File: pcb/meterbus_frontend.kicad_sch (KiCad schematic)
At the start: 32 parts, among them J2 6P6C, Q1 SQ2308CES-T1_GE3, U1 L7805, U2 74HC132, U3 ISO6721RBD

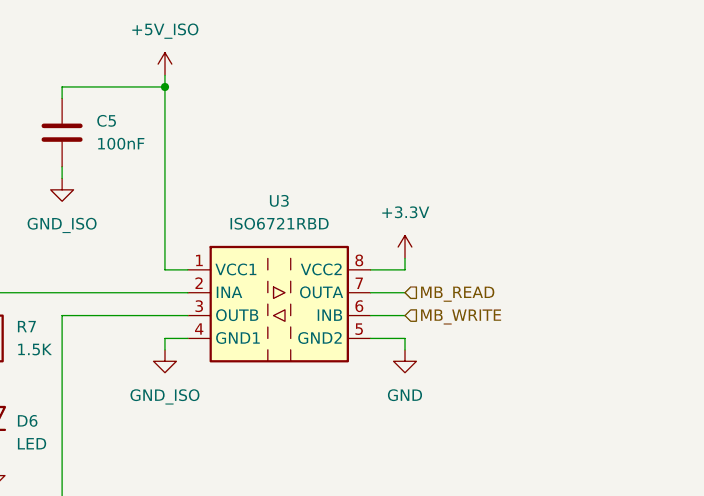
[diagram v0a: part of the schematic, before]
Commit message: feat: add W5500 ethernet controller
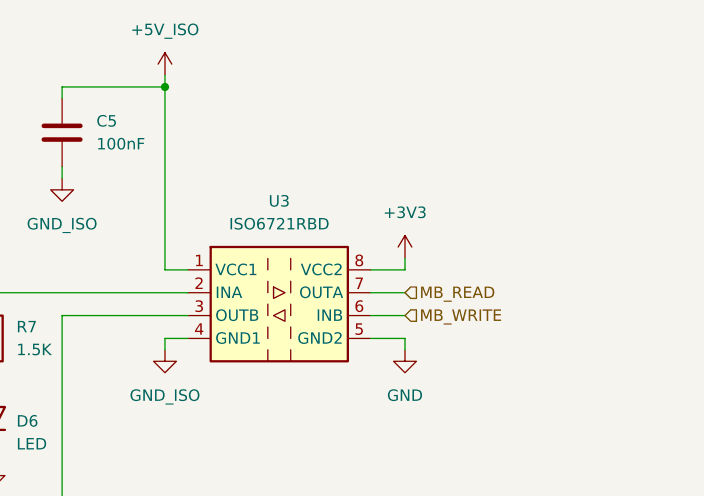
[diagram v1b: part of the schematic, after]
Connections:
- net +3.3V renamed +3V3
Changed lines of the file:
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@@
+	)
+	(symbol
+		(lib_id "power:+3V3")
+		(at 243.84 49.53 0)
+		(unit 1)
+		(body_style 1)
+		(exclude_from_sim no)
+		(in_bom yes)
+		(on_board yes)
+		(in_pos_files yes)
+		(dnp no)
+		(fields_autoplaced yes)
+		(property "Reference" "#PWR021"
+			(at 243.84 53.34 0)
+			(hide yes)
+			(show_name no)
+			(do_not_autoplace no)
+			(effects
+				(font
+					(size 1.27 1.27)
+				)
+			)
+		)
+		(property "Value" "+3V3"
+			(at 243.84 44.45 0)
+			(show_name no)
+			(do_not_autoplace no)
+			(effects
+				(font
+					(size 1.27 1.27)
+				)
+			)
+		)
+		(property "Footprint" ""
+			(at 243.84 49.53 0)
+			(hide yes)
+			(show_name no)
+			(do_not_autoplace no)
+			(effects
+				(font
+					(size 1.27 1.27)
+				)
+			)
+		)
+		(property "Datasheet" ""
+			(at 243.84 49.53 0)
+			(hide yes)
+			(show_name no)
+			(do_not_autoplace no)
+			(effects
+				(font
+					(size 1.27 1.27)
+				)
+			)
+		)
+		(property "Description" "Power symbol creates a global label with name \"+3V3\""
+			(at 243.84 49.53 0)
+			(hide yes)
+			(show_name no)
+			(do_not_autoplace no)
+			(effects
+				(font
+					(size 1.27 1.27)
+				)
+			)
+		)
+		(pin "1"
+		)
+		(instances
+			(project "EveningStar"
+				(path "/4c61f5a2-f8d4-462a-9bc3-d74437d30372/20698281-7733-498d-8537-9736b11e1ce7"
+					(reference "#PWR021")
+					(unit 1)
+				)
+			)
+		)
 	)
 	(symbol
@@
 					(unit 1)
 				)
-			)
-		)
-	)
-	(symbol
-		(lib_id "power:+3.3V")
-		(at 243.84 49.53 0)
-		(unit 1)
-		(body_style 1)
-		(exclude_from_sim no)
-		(in_bom yes)
-		(on_board yes)
-		(in_pos_files yes)
-		(dnp no)
-		(fields_autoplaced yes)
-		(property "Reference" "#PWR021"
-			(at 243.84 53.34 0)
-			(hide yes)
-			(show_name no)
-			(do_not_autoplace no)
-			(effects
-				(font
-					(size 1.27 1.27)
-				)
-			)
-		)
-		(property "Value" "+3.3V"
-			(at 243.84 44.45 0)
-			(show_name no)
-			(do_not_autoplace no)
-			(effects
-				(font
-					(size 1.27 1.27)
-				)
-			)
-		)
-		(property "Footprint" ""
-			(at 243.84 49.53 0)
-			(hide yes)
-			(show_name no)
-			(do_not_autoplace no)
-			(effects
-				(font
-					(size 1.27 1.27)
-				)
-			)
-		)
-		(property "Datasheet" ""
-			(at 243.84 49.53 0)
-			(hide yes)
-			(show_name no)
-			(do_not_autoplace no)
-			(effects
-				(font
-					(size 1.27 1.27)
-				)
-			)
-		)
-		(property "Description" "Power symbol creates a global label with name \"+3.3V\""
-			(at 243.84 49.53 0)
-			(hide yes)
-			(show_name no)
-			(do_not_autoplace no)
-			(effects
-				(font
-					(size 1.27 1.27)
-				)
-			)
-		)
-		(pin "1"
-		)
-		(instances
-			(project "EveningStar"
-				(path "/4c61f5a2-f8d4-462a-9bc3-d74437d30372/20698281-7733-498d-8537-9736b11e1ce7"
-					(reference "#PWR021")
-					(unit 1)
-				)

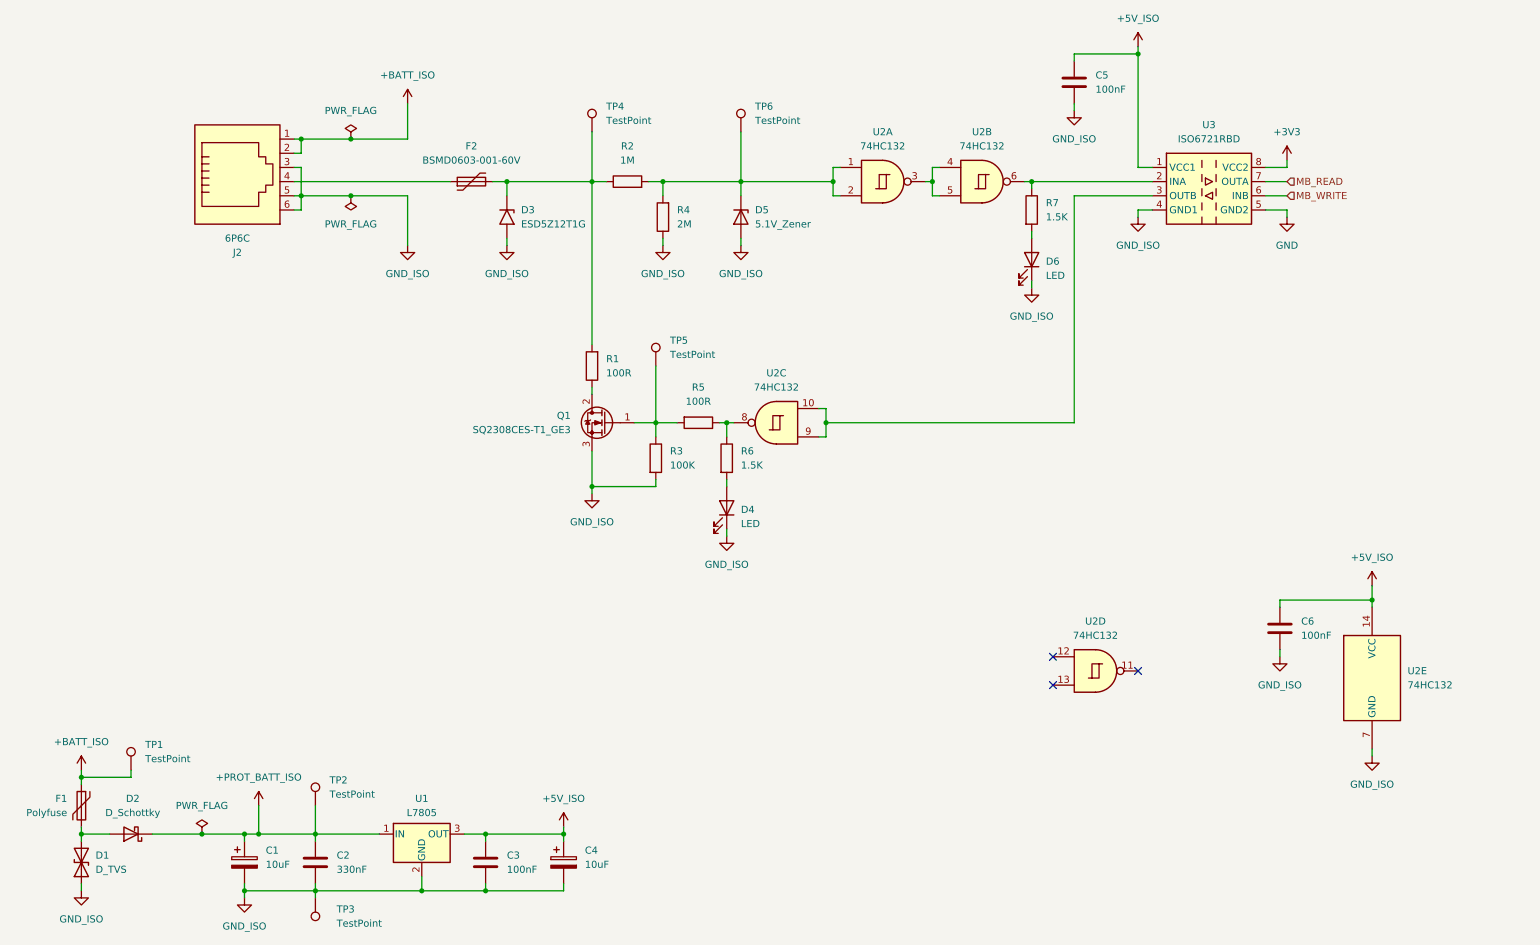
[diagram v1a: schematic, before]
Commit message: feat: connect ethernet to mcu and sort erc errors
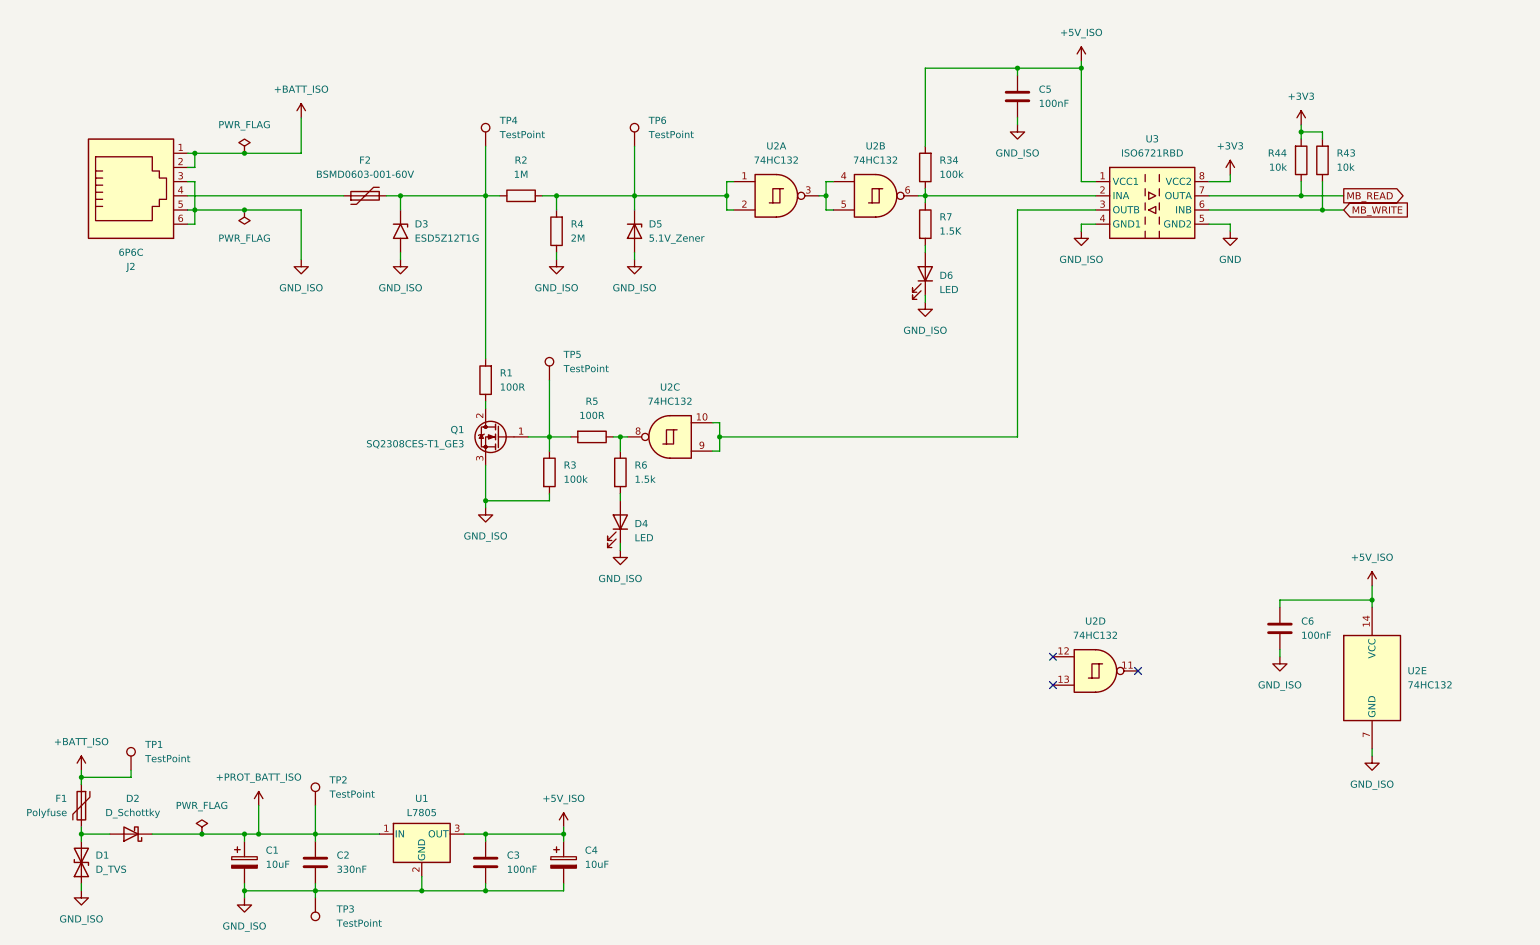
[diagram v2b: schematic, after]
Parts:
- added R34: 100k, symbol Device:R
- added R43, R44: 10k, symbol Device:R
- R3: value 100K -> 100k
- R6: value 1.5K -> 1.5k
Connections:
- net +3V3: now also R43.2, R44.2
- net +5V_ISO: now also R34.2
- net MB_READ: now also R44.1
- net MB_WRITE: now also R43.1
- net at R7.1, U2.6, U3.2 (INA): now also R34.1
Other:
- moved on the sheet: C5, D3, D4, D5, D6, F2, J2, Q1, R1, R2, R3, R4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

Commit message: feat: update compoents with lcsc parts
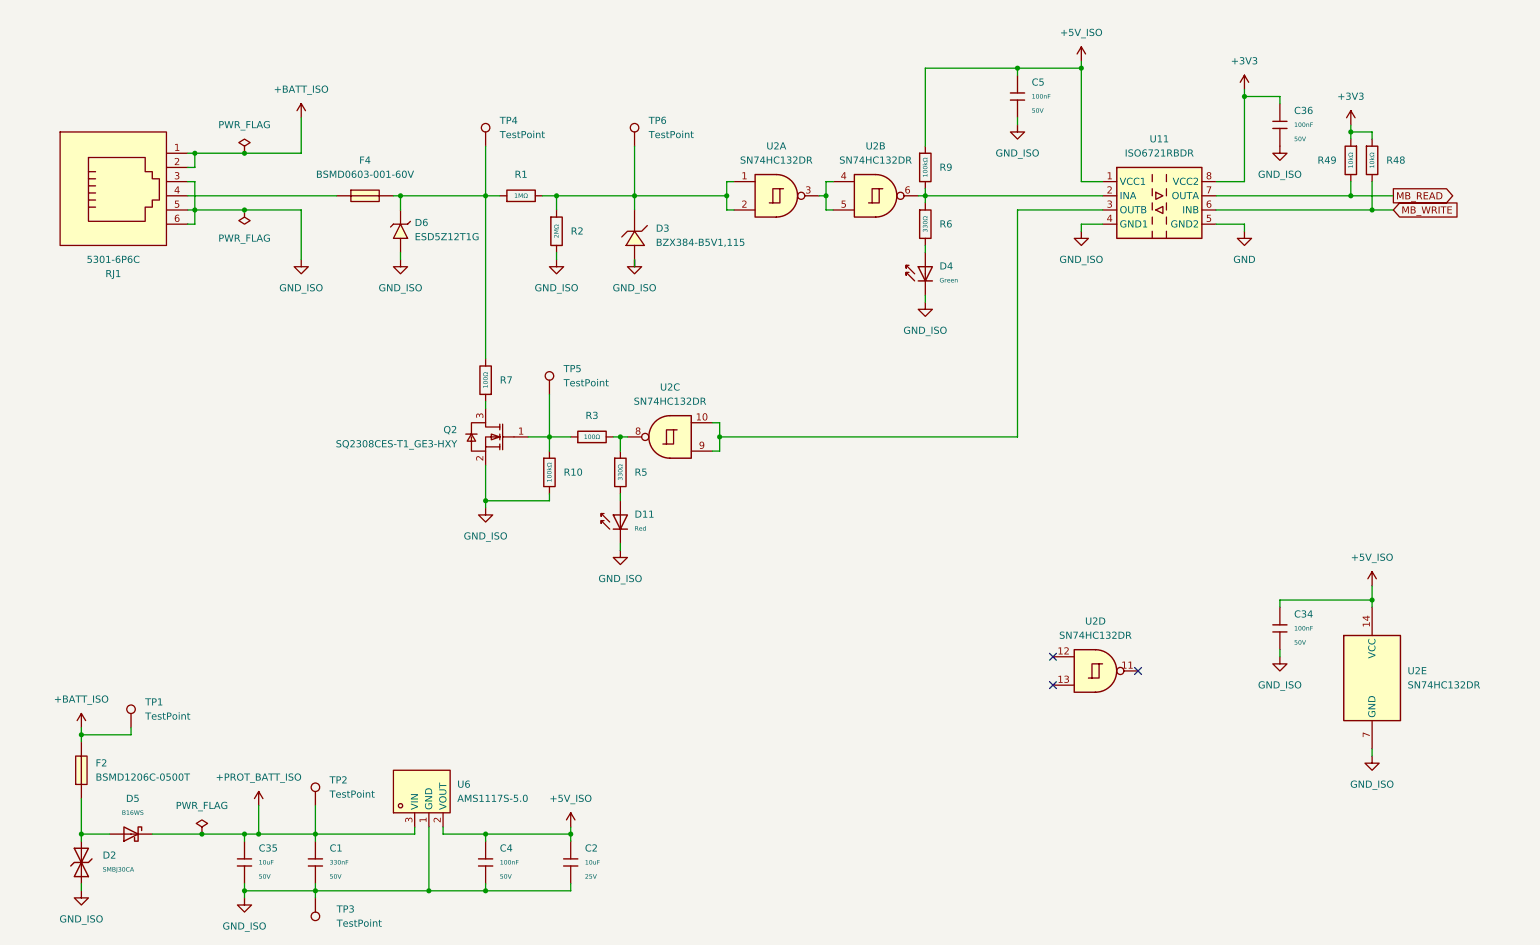
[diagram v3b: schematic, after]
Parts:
- removed C1, C4: 10uF, symbol Device:C_Polarized
- removed C2: 330nF, symbol Device:C
- removed C3, C5, C6: 100nF, symbol Device:C
- removed D1: D_TVS, symbol Device:D_TVS
- removed D2: D_Schottky, symbol Device:D_Schottky
- removed D3: ESD5Z12T1G, Diode_SMD:D_SOD-523, symbol Diode:SM6T15A
- removed D4, D6: LED, symbol Device:LED
- removed D5: 5.1V_Zener, symbol Device:D_Zener
- removed F1: Polyfuse, symbol Device:Polyfuse
- removed F2: BSMD0603-001-60V, Fuse:Fuse_0603_1608Metric_Pad1.05x0.95mm_HandSolder, symbol Device:Polyfuse
- removed J2: 6P6C, symbol Connector:6P6C
- removed Q1: SQ2308CES-T1_GE3, Package_TO_SOT_SMD:SOT-23, symbol custom_symbols:IRLL014NTRPBF
- removed R1, R5: 100R, symbol Device:R
- removed R2: 1M, symbol Device:R
- removed R3, R34: 100k, symbol Device:R
- removed R4: 2M, symbol Device:R
- removed R43, R44: 10k, symbol Device:R
- removed R6: 1.5k, symbol Device:R
- removed R7: 1.5K, symbol Device:R
- removed U1: L7805, symbol Regulator_Linear:L7805
- removed U3: ISO6721RBD, Package_SO:SOIC-8_3.9x4.9mm_P1.27mm, symbol Isolator:ISO6721RBD
- added C1: 330nF, PCM_JLCPCB:C_0805, symbol PCM_JLCPCB-Capacitors:0805,330nF
- added C2: 10uF, PCM_JLCPCB:C_0603, symbol PCM_JLCPCB-Capacitors:0603,10uF,(2)
- added C34, C36, C4, C5: 100nF, PCM_JLCPCB:C_0603, symbol PCM_JLCPCB-Capacitors:0603,100nF
- added C35: 10uF, PCM_JLCPCB:C_1206, symbol PCM_JLCPCB-Capacitors:1206,10uF
- added D11: Red, PCM_JLCPCB:D_0805, symbol PCM_JLCPCB-Diodes:LED,0805,Red
- added D2: SMBJ30CA, PCM_JLCPCB:D_SMB, symbol PCM_JLCPCB-Diodes:TVS-Bi,SMBJ30CA
- added D3: BZX384-B5V1,115, EasyEDA:SOD-323_L1.7-W1.3-LS2.5-RD, symbol EasyEDA:BZX384-B5V1,115
- added D4: Green, PCM_JLCPCB:D_0805, symbol PCM_JLCPCB-Diodes:LED,0805,Green
- added D5: B16WS, PCM_JLCPCB:D_SOD-323, symbol PCM_JLCPCB-Diodes:Schottky,B16WS
- added D6: ESD5Z12T1G, EasyEDA:SOD-523F_L1.2-W0.8-LS1.7-RD, symbol EasyEDA:ESD5Z12T1G
- added F2: BSMD1206C-0500T, EasyEDA:F1206, symbol EasyEDA:BSMD1206C-0500T
- added F4: BSMD0603-001-60V, EasyEDA:F0603, symbol EasyEDA:BSMD0603-001-60V
- added Q2: SQ2308CES-T1_GE3-HXY, EasyEDA:SOT-23-3_L3.0-W1.7-P0.95-LS2.9-BR, symbol EasyEDA:SQ2308CES-T1_GE3-HXY
- added R1: 1MΩ, PCM_JLCPCB:R_0603, symbol PCM_JLCPCB-Resistors:0603,1MΩ
- added R10, R9: 100kΩ, PCM_JLCPCB:R_0603, symbol PCM_JLCPCB-Resistors:0603,100kΩ
- added R2: 2MΩ, PCM_JLCPCB:R_0603, symbol PCM_JLCPCB-Resistors:0603,2MΩ
- added R3, R7: 100Ω, PCM_JLCPCB:R_0603, symbol PCM_JLCPCB-Resistors:0603,100Ω
- added R48, R49: 10kΩ, PCM_JLCPCB:R_0603, symbol PCM_JLCPCB-Resistors:0603,10kΩ
- added R5, R6: 330Ω, PCM_JLCPCB:R_0603, symbol PCM_JLCPCB-Resistors:0603,330Ω
- added RJ1: 5301-6P6C, EasyEDA:RJ45-TH_5301-6P6C, symbol EasyEDA:5301-6P6C
- added U11: ISO6721RBDR, EasyEDA:SOP-8_L4.9-W3.9-P1.27-LS6.0-BL_ISO6721RBDR, symbol Isolator:ISO6721RBD
- added U6: AMS1117S-5.0, EasyEDA:SOT-89-3_L4.5-W2.5-P1.50-LS4.2-BR, symbol EasyEDA:AMS1117S-5.0
- TP1, TP2, TP3, TP4, TP5, TP6: footprint (none) -> EasyEDA:TEST-TH_BD2.54-P1.4_BLACK; LCSC Part (none) -> C5199801; MPN (none) -> RH-5001
- U2: value 74HC132 -> SN74HC132DR; footprint (none) -> EasyEDA:SOIC-14_L8.7-W3.9-P1.27-LS6.0-BL; LCSC Part (none) -> C350560; MPN (none) -> SN74HC132DR
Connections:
- net +3V3: now also C36.1, R48.1, R49.1, U11.8 (VCC2)
- net +5V_ISO: now also C2.1, C34.1, C4.1, C5.1, R9.1, U11.1 (VCC1), U6.2 (VOUT)
- net +BATT_ISO: now also F2.2, RJ1.1, RJ1.2
- net +PROT_BATT_ISO: now also C1.1, C35.1, D5.1, U6.3 (VIN)
- net GND: now also U11.5 (GND2)
- net GND_ISO: now also C1.2, C2.2, C34.2, C35.2, C36.2, C4.2, C5.2, D11.1, D2.1, D3.2 (A), D4.1, D6.2 (Anode), Q2.2 (S), R10.2, R2.2, RJ1.3, RJ1.5, RJ1.6, U11.4 (GND1), U6.1 (GND)
- net MB_READ: now also R49.2, U11.7 (OUTA)
- net MB_WRITE: now also R48.2, U11.6 (INB)
- net at TP6.1, U2.1, U2.2: now also D3.1 (C), R1.2, R2.1
- net at TP4.1: now also D6.1 (Cathode), F4.2, R1.1, R7.2
- net at U2.8: now also R3.2, R5.1
- net at TP5.1: now also Q2.1 (G), R10.1, R3.1
- net at U2.6: now also R6.1, R9.2, U11.2 (INA)
- net at U2.10, U2.9: now also U11.3 (OUTB)
- new net: Q2.3 (D), R7.1
- new net: D11.2, R5.2
- new net: D2.2, D5.2, F2.1
- new net: F4.1, RJ1.4
- new net: D4.2, R6.2
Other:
- moved on the sheet: TP1, TP5

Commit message: feat: layout meterbus frontend
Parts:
- added TP12: BUS, EasyEDA:TEST-TH_BD2.54-P1.4_BLACK, symbol Connector:TestPoint
- added TP13: 5V_ISO, EasyEDA:TEST-TH_BD2.54-P1.4_BLACK, symbol Connector:TestPoint
- added TP14: RX_MB, EasyEDA:TEST-TH_BD2.54-P1.4_BLACK, symbol Connector:TestPoint
- added TP15: TX_MB, EasyEDA:TEST-TH_BD2.54-P1.4_BLACK, symbol Connector:TestPoint
- added TP16: TX_MCU, EasyEDA:TEST-TH_BD2.54-P1.4_BLACK, symbol Connector:TestPoint
- added TP17: RX_MCU, EasyEDA:TEST-TH_BD2.54-P1.4_BLACK, symbol Connector:TestPoint
- D4: renamed from D11; value Red -> TX
- D6: renamed from D4; value Green -> RX
- TP1: value TestPoint -> BAT_ISO
- TP2: value TestPoint -> BAT_ISO_PROT
- TP3: value TestPoint -> GND_ISO
- TP4: value TestPoint -> BUS_PROT
- TP5: value TestPoint -> TX_GATE
- TP6: value TestPoint -> RX_DIV
- renumbered C35 to C1, C1 to C2, C4 to C3, C2 to C4, C36 to C6, C34 to C7, D2 to D1, D5 to D2, D6 to D3, D3 to D5, F2 to F1, F4 to F2, Q2 to Q1, R7 to R1, R48 to R10, R1 to R2, R10 to R3, R2 to R4, R3 to R5, R5 to R6, R9 to R7, R6 to R8, R49 to R9, U6 to U1, U11 to U3
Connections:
- net +5V_ISO: now also TP13.1
- net GND: now also C6.2
- net GND_ISO: no longer C6.2
- net MB_READ: now also TP17.1
- net MB_WRITE: now also TP16.1
- net at R7.2, R8.1, U2.6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: now also TP14.1
- net at F2.1, RJ1.4: now also TP12.1
- net at U2.10, U2.9, U3.3 (OUTB): now also TP15.1
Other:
- moved on the sheet: C3, C4, R10, R9, U1

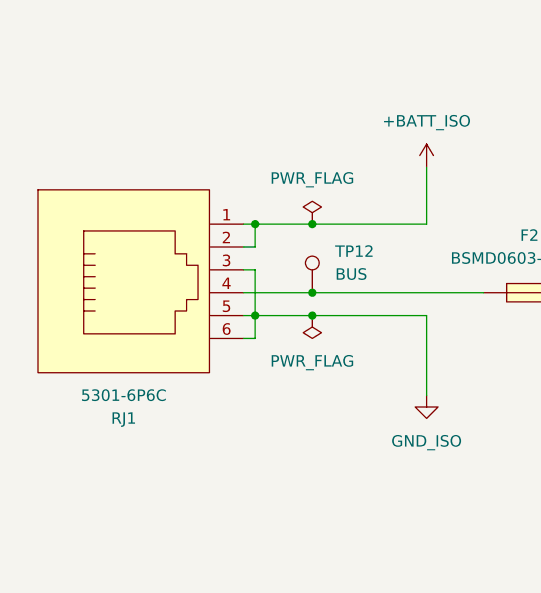
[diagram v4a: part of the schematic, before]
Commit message: fix: flip rj11 meterbus connector
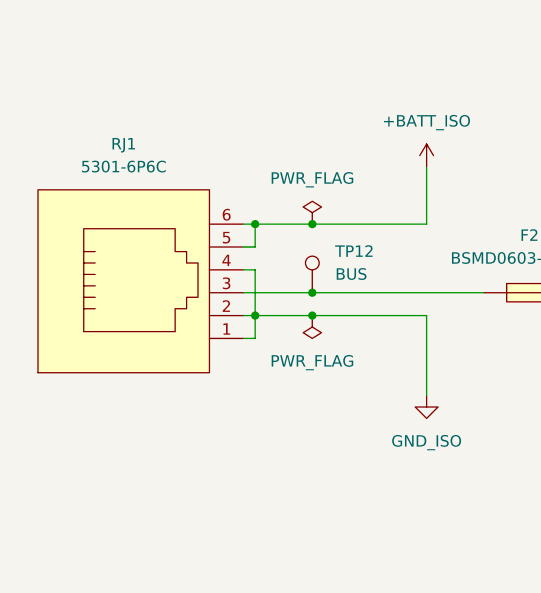
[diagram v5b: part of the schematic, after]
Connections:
- net +BATT_ISO: now also RJ1.5, RJ1.6; no longer RJ1.1, RJ1.2
- net GND_ISO: now also RJ1.1, RJ1.2, RJ1.4; no longer RJ1.3, RJ1.5, RJ1.6
- net at F2.1, TP12.1: now also RJ1.3; no longer RJ1.4
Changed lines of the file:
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@@
 		(lib_id "EasyEDA:5301-6P6C")
 		(at 35.56 54.61 90)
-		(mirror x)
 		(unit 1)
 		(body_style 1)
@@
 		(dnp no)
 		(property "Reference" "RJ1"
-			(at 33.655 69.85 90)
+			(at 33.655 39.37 90)
 			(show_name no)
 			(do_not_autoplace no)
@@
 		)
 		(property "Value" "5301-6P6C"
-			(at 33.655 67.31 90)
+			(at 33.655 41.91 90)
 			(show_name no)
 			(do_not_autoplace no)

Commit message: feat: create pcb production files and swap some parts for basic
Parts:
- removed C2: 330nF, PCM_JLCPCB:C_0805, symbol PCM_JLCPCB-Capacitors:0805,330nF
- removed U1: AMS1117S-5.0, EasyEDA:SOT-89-3_L4.5-W2.5-P1.50-LS4.2-BR, symbol EasyEDA:AMS1117S-5.0
- added C35: 100nF, PCM_JLCPCB:C_0603, symbol PCM_JLCPCB-Capacitors:0603,100nF
- added U10: AMS1117-5.0, EasyEDA:SOT-223_L6.5-W3.5-P2.30-LS7.0-BR, symbol EasyEDA:AMS1117-5.0
- TP1: value BAT_ISO -> RH-5001
- TP12: value BUS -> RH-5001
- TP13: value 5V_ISO -> RH-5001
- TP14: value RX_MB -> RH-5001
- TP15: value TX_MB -> RH-5001
- TP16: value TX_MCU -> RH-5001
- TP17: value RX_MCU -> RH-5001
- TP2: value BAT_ISO_PROT -> RH-5001
- TP3: value GND_ISO -> RH-5001
- TP4: value BUS_PROT -> RH-5001
- TP5: value TX_GATE -> RH-5001
- TP6: value RX_DIV -> RH-5001
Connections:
- net +5V_ISO: now also U10.2 (VOUT)
- net +PROT_BATT_ISO: now also C35.1, U10.3 (VIN)
- net GND_ISO: now also C35.2, U10.1 (GND)
